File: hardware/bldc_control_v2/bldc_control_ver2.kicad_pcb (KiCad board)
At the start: 2 copper layers, 98 x 38 mm, 69 parts, among them IC1 6N136, IC2 6N136, IC3 6N136, IC4 6N136, IC5 6N136, P1 CONN_01X04, P2 CONN_01X03, P3 CONN_01X06, P4 CONN_01X08, P5 CONN_01X04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

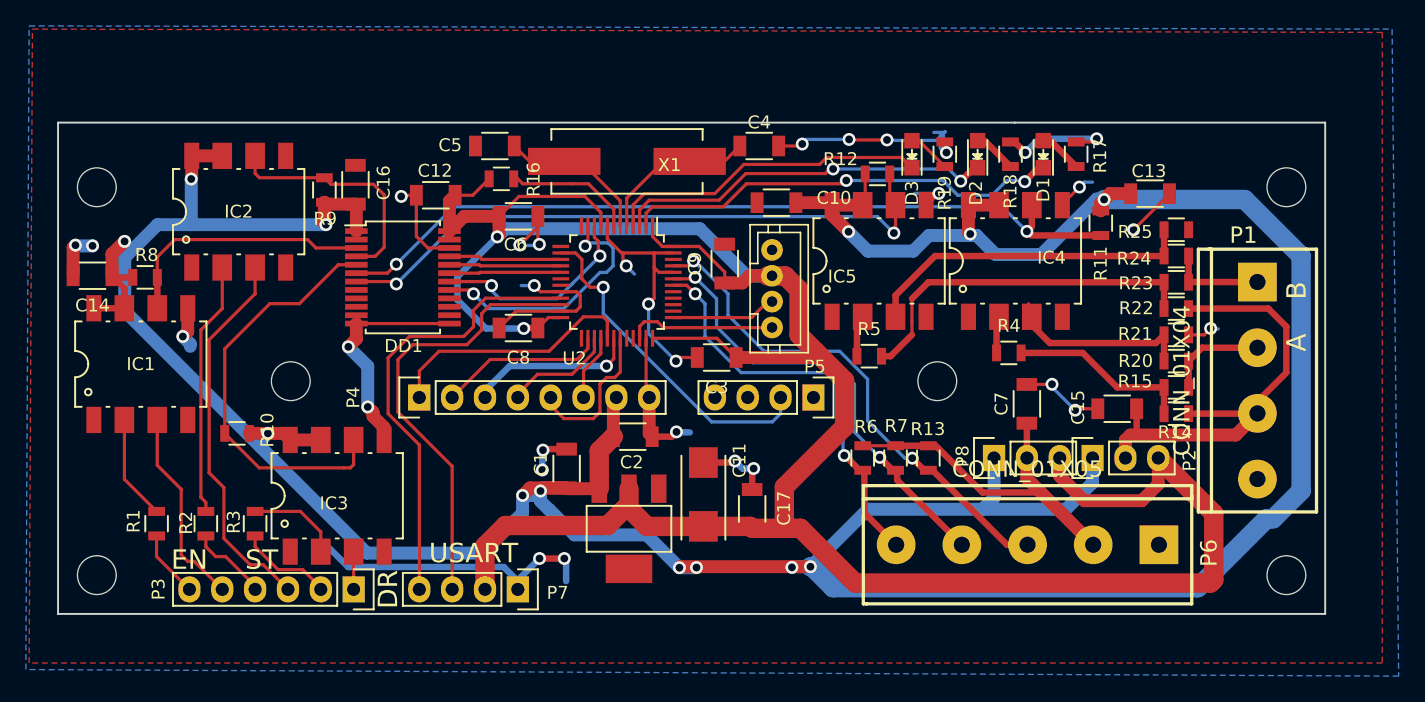
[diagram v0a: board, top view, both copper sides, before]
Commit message: schaltplan und layout angepasst
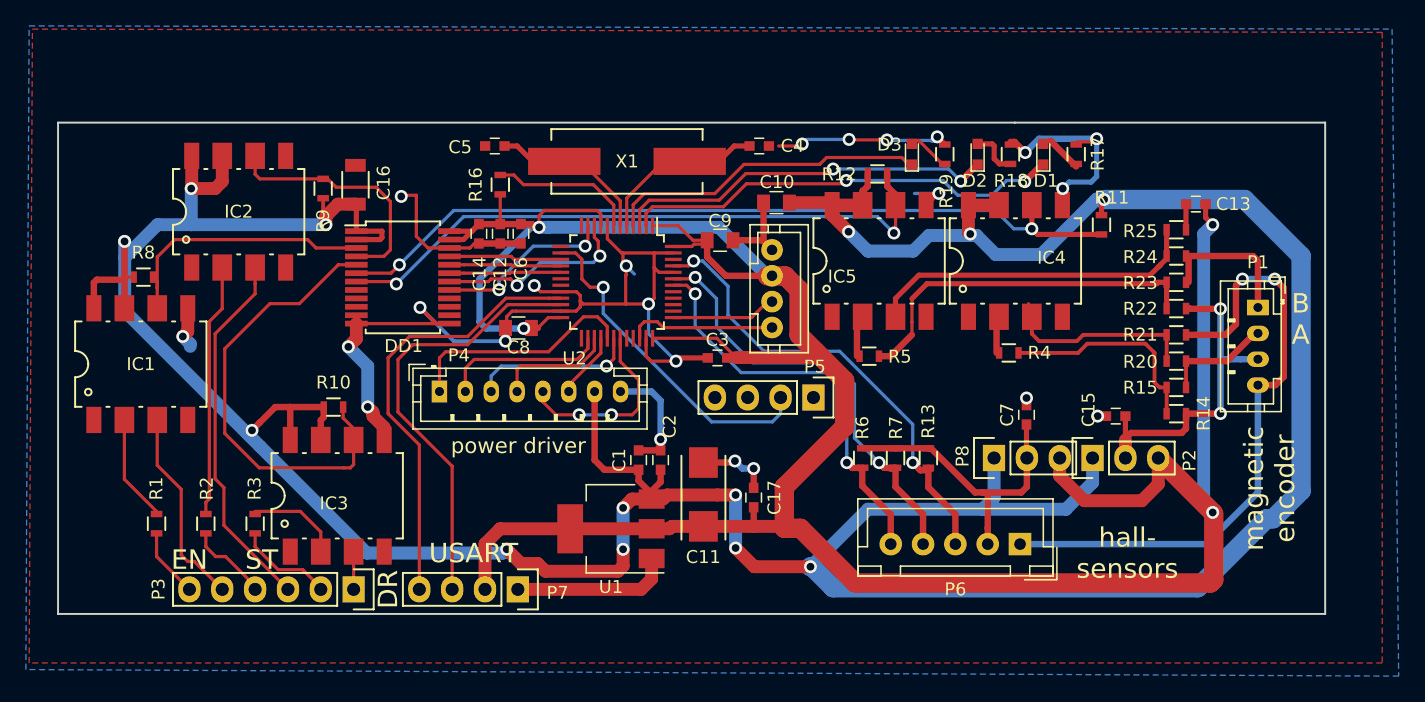
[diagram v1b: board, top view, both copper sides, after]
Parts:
- removed REF** (x6): MountingHole_3mm, Mounting_Holes:MountingHole_3mm
- C1, C12, C13, C14, C15, C17, C2, C3, C6, C7: value C -> 100n; footprint Capacitors_SMD:C_1206 -> Capacitors_SMD:C_0603
- C10, C8, C9: value C -> 10µ; footprint Capacitors_SMD:C_1206 -> Capacitors_SMD:C_0805
- C16: value C -> 100n
- C4, C5: value C -> 18p; footprint Capacitors_SMD:C_1206 -> Capacitors_SMD:C_0603
- D1, D2, D3: footprint LEDs:LED-0805 -> LEDs:LED_0603
- P1: footprint w_conn_screw:mors_4p -> Connectors_JST:JST_PH_B4B-PH-K_04x2.00mm_Straight
- P4: footprint Pin_Headers:Pin_Header_Straight_1x08 -> Connectors_JST:JST_PH_B8B-PH-K_08x2.00mm_Straight
- P6: footprint w_conn_screw:mors_5p -> Connectors_JST:JST_XH_B05B-XH-A_05x2.50mm_Straight
- R1, R17, R18, R19, R2, R3, R4, R5: value R -> 220; footprint Resistors_SMD:R_0805 -> Resistors_SMD:R_0603
- R10, R11, R12, R13, R16, R6, R7, R8, R9: value R -> 10k; footprint Resistors_SMD:R_0805 -> Resistors_SMD:R_0603
- R14, R15, R20, R21, R22, R23, R24, R25: footprint Resistors_SMD:R_0805 -> Resistors_SMD:R_0603
- U1: footprint acronet:SOT223_S -> TO_SOT_Packages_SMD:SOT-223-3Lead_TabPin2
- X1: value CRYSTAL -> 8MHz
- moved C14 30.1 mm to (178.6, 96.6), turned to 270 degrees
- moved R10 7.73 mm to (167.3, 110.0)
- moved C12 5.81 mm to (180.2, 96.6), turned to 270 degrees
- moved P1 5.65 mm to (238.8, 102.3)
- moved C1 5.61 mm to (190.9, 114.1)
- moved C13 3.64 mm to (234.0, 94.3), turned to 180 degrees
- moved C2 2.81 mm to (192.6, 114.1), turned to 90 degrees
- moved C9 1.84 mm to (197.2, 97.1), turned to 0 degrees
- moved P4 1.63 mm to (175.5, 108.8), turned to 0 degrees
- moved U1 1.40 mm to (188.8, 119.4)
- moved C6 1.36 mm to (181.8, 96.6), turned to 270 degrees
- moved C17 0.88 mm to (199.8, 117.0)
- moved C7 0.85 mm to (220.9, 110.6)
- moved P6 0.58 mm to (220.4, 120.6)
- moved C15 0.58 mm to (227.8, 110.7), turned to 0 degrees
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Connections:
- C11 pad 1: +3.3V -> +3V3
- C12 pad 1: +3.3V -> +3V3
- C13 pad 1: +5V -> +3V3
- C14 pad 1: +5V -> +3V3
- C15 pad 1: /ENC_SUPPLY -> GND
- C15 pad 2: GND -> /ENC_SUPPLY
- C17 pad 1: +3.3V -> +3V3
- C3 pad 1: +3.3V -> +3V3
- C6 pad 1: +3.3V -> +3V3
- C8 pad 1: +3.3V -> +3V3
- C9 pad 1: +3.3V -> +3V3
- DD1 pad 10: (no net) -> Net-(DD1-Pad10)
- DD1 pad 14: (no net) -> Net-(DD1-Pad14)
- DD1 pad 15: (no net) -> Net-(DD1-Pad15)
- DD1 pad 16: (no net) -> Net-(DD1-Pad16)
- DD1 pad 23: +3.3V -> +3V3
- DD1 pad 24: +3.3V -> +3V3
- DD1 pad 8: (no net) -> Net-(DD1-Pad8)
- DD1 pad 9: (no net) -> Net-(DD1-Pad9)
- P2 pad 3: +3.3V -> +3V3
- P5 pad 3: (no net) -> Net-(P5-Pad3)
- P5 pad 4: (no net) -> Net-(P5-Pad4)
- P7 pad 2: +3.3V -> +3V3
- P8 pad 3: +3.3V -> +3V3
- P9 pad 3: +3.3V -> +3V3
- R10 pad 1: /DIR -> +5V
- R10 pad 2: +5V -> /DIR
- R11 pad 1: /ENC_A -> +5V
- R11 pad 2: +5V -> /ENC_A
- R12 pad 1: /ENC_B -> +5V
- R12 pad 2: +5V -> /ENC_B
- R16 pad 1: +3.3V -> +3V3
- R8 pad 1: /ENA -> +5V
- R8 pad 2: +5V -> /ENA
- R9 pad 1: /STEP -> +5V
- R9 pad 2: +5V -> /STEP
- U1 pad 2: +3.3V -> +3V3
- U2 pad 1: +3.3V -> +3V3
- U2 pad 12: (no net) -> Net-(U2-Pad12)
- U2 pad 13: (no net) -> Net-(U2-Pad13)
- U2 pad 18: (no net) -> Net-(U2-Pad18)
- U2 pad 19: (no net) -> Net-(U2-Pad19)
- U2 pad 24: +3.3V -> +3V3
- U2 pad 25: (no net) -> Net-(U2-Pad25)
- U2 pad 32: (no net) -> Net-(U2-Pad32)
- U2 pad 33: (no net) -> Net-(U2-Pad33)
- U2 pad 36: +3.3V -> +3V3
- U2 pad 38: (no net) -> /TDI
- U2 pad 39: (no net) -> Net-(U2-Pad39)
- U2 pad 40: (no net) -> Net-(U2-Pad40)
- U2 pad 41: (no net) -> Net-(U2-Pad41)
- U2 pad 46: (no net) -> Net-(U2-Pad46)
- U2 pad 48: +3.3V -> +3V3
- U2 pad 9: +3.3V -> +3V3
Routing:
- net +3V3: track 0.00 -> 222.3 mm, vias 0 -> 4
- net +3.3V: track 199.6 -> 0.00 mm, vias 2 -> 0
- net GND: track 163.5 -> 215.6 mm, vias 31 -> 25
- net +5V: track 290.7 -> 305.7 mm
- net /ENC_SUPPLY: track 35.6 -> 28.7 mm, vias 0 -> 2
- net /ENC_B_3V3: track 20.5 -> 14.0 mm
- net /B_IN: track 7.36 -> 11.4 mm
- net /HALL_SUPPLY: track 26.8 -> 23.1 mm
- net Net-(C4-Pad1): track 12.6 -> 16.0 mm
- net /H_C: track 11.8 -> 14.8 mm, vias 0 -> 2
- net /DIR: track 32.5 -> 35.4 mm
- net /HALL_C: track 39.5 -> 36.7 mm
- net Net-(R14-Pad1): track 14.2 -> 16.5 mm
- net /H_A: track 19.8 -> 18.1 mm
- net /ENA: track 22.6 -> 21.2 mm
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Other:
- board text added: "B A"
- board text added: "BLDC Controller REV2.1 (C) Pekka Roivainen"
- board text added: "hall- sensors"
- board text added: "magnetic encoder"
- board text added: "power driver"
- board text removed: "A B"
- board text removed: "BLDC Controller REV2 (C) Pekka Roivainen"
